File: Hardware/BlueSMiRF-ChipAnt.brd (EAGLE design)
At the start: 41.9 x 16 mm, 27 parts, among them Q1 MOSFET-NCHANNELSMD, Q2 MOSFET-NCHANNELSMD, U1 BLUETOOTH-RN41, U3 3.3V

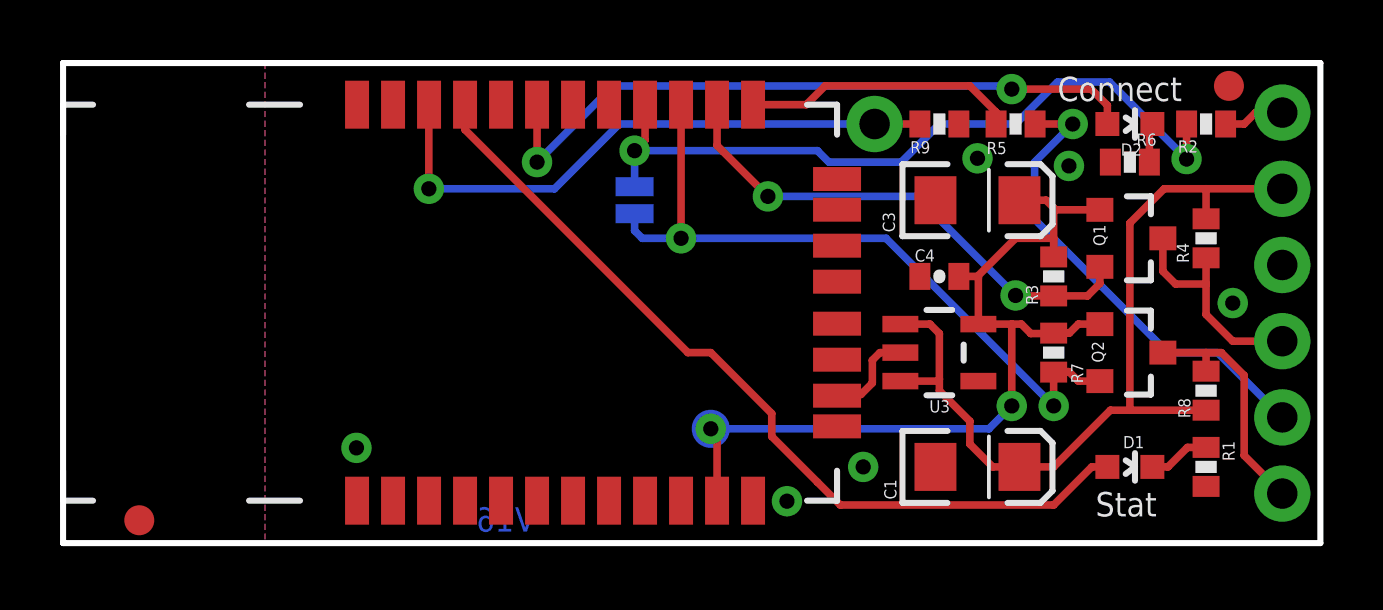
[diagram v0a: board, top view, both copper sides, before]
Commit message: Update RES/CAP packages to 0603
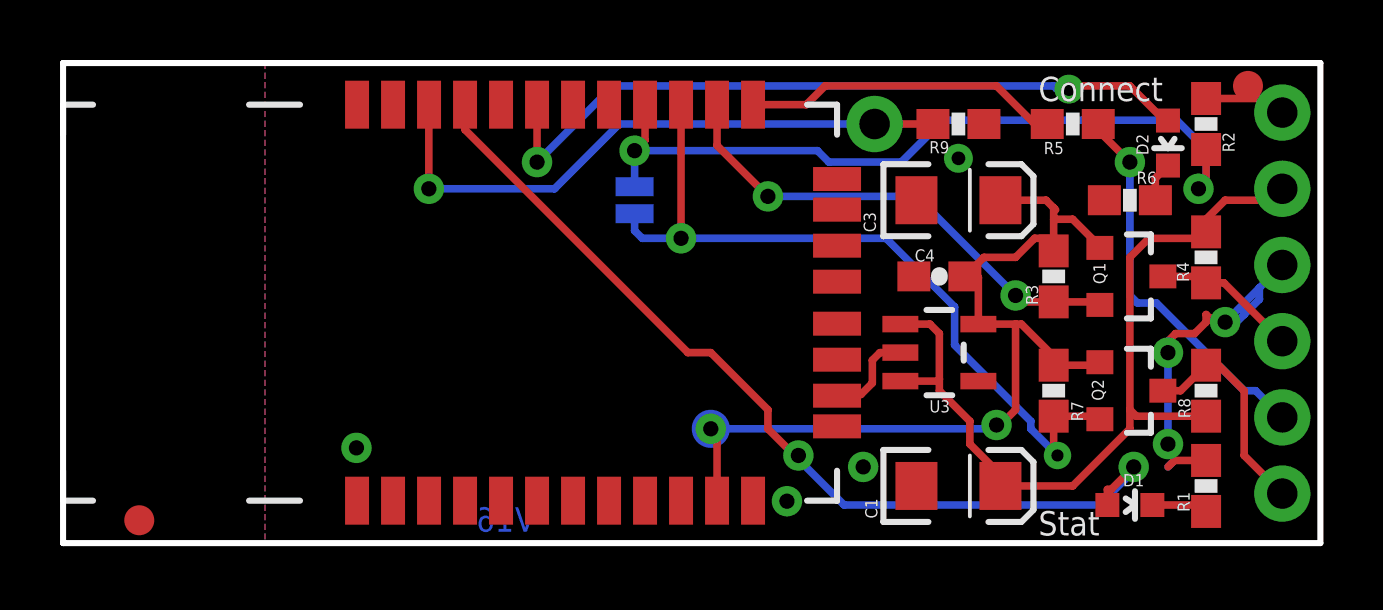
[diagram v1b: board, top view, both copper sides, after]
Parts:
- C4: device SparkFun:0402-CAP -> SparkFun:0603-CAP
- R1, R2, R3, R4, R5, R6, R7, R8, R9: device SparkFun:0402-RES -> SparkFun:0603-RES
- moved R5 1.91 mm to (33.7, 14.0)
- moved D2 1.42 mm to (36.8, 13.3), turned to 180 degrees
- moved D1 1.27 mm to (35.6, 1.27)
- moved Q1 1.27 mm to (35.6, 8.89)
- moved Q2 1.27 mm to (35.6, 5.08)
- moved R6 1.27 mm to (35.6, 11.4)
- moved R7 1.27 mm to (33.0, 5.08)
- moved C1 0.90 mm to (29.8, 1.91)
- moved C3 0.64 mm to (29.8, 11.4)
- moved R1 0.64 mm to (38.1, 1.91), turned to 90 degrees
- moved R4 0.63 mm to (38.1, 9.53)
- moved JP3 0.63 mm to (39.5, 15.2)
- moved R9 0.63 mm to (29.8, 14.0)
- turned R2 to 90 degrees
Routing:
- net GND: track 3.15 -> 14.5 mm, vias 6 -> 7
- net RX_5V: track 15.9 -> 12.9 mm
- net N$1: track 28.4 -> 31.1 mm, vias 0 -> 2
- net TX_5V: track 7.51 -> 4.87 mm
- net 3.3V: track 29.6 -> 31.9 mm
- net RTS: track 24.2 -> 26.1 mm
- net N$2: track 22.9 -> 24.6 mm
- net RX: track 9.12 -> 10.6 mm
- net CTS: track 24.8 -> 25.9 mm
- net CTS_5V: track 2.05 -> 2.73 mm
- net TX: track 16.9 -> 16.3 mm

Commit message: Updated board layout
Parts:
- removed JP3: FIDUCIAL1X2, SparkFun:FIDUCIAL-1X2
- moved D1 2.44 mm to (37.5, 2.79)
- moved R2 1.14 mm to (37.5, 14.9), turned to 0 degrees
- moved R1 0.90 mm to (37.5, 1.27), turned to 180 degrees
- moved D2 0.65 mm to (37.5, 13.5), turned to 90 degrees
- moved R4 0.63 mm to (38.1, 8.89)
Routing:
- net GND: track 14.5 -> 5.69 mm, vias 7 -> 4
- net N$2: track 24.6 -> 28.7 mm
- net 3.3V: track 31.9 -> 28.7 mm
- net CTS: track 25.9 -> 23.5 mm
- net D2: track 1.33 -> 2.57 mm
- net RX_5V: track 12.9 -> 14.0 mm
- net RTS: track 26.1 -> 25.2 mm

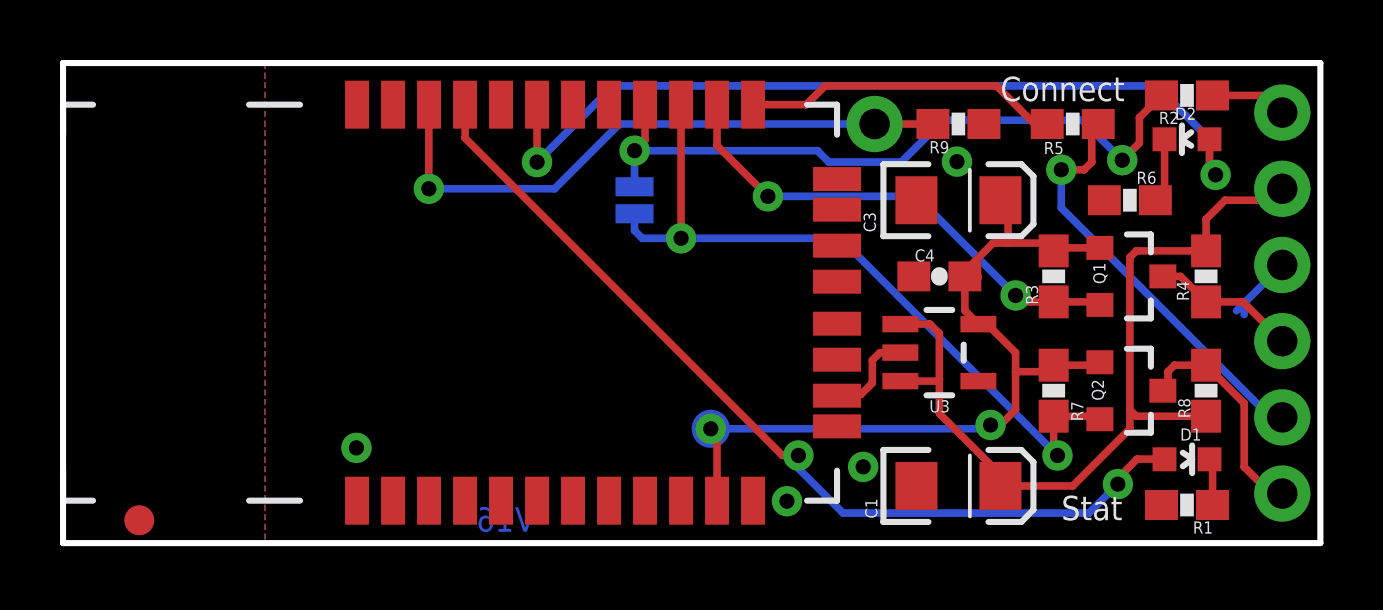
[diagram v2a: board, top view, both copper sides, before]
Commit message: Fixing silk screen positions
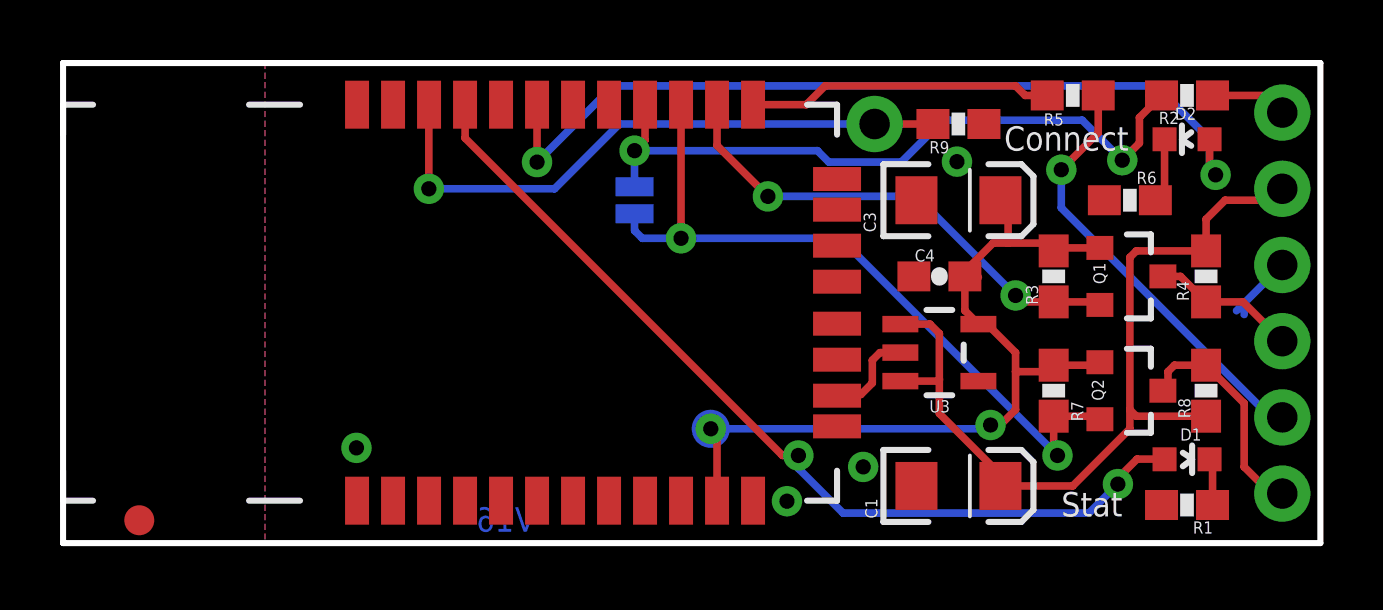
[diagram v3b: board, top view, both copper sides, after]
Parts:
- added U$2: REVISION, SparkFun-Aesthetics:REVISION
- moved R5 0.95 mm to (33.7, 14.9)
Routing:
- net RX_5V: track 14.0 -> 14.5 mm
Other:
- board text added: "J. Lindblom"
- board text added: "T. Klopfenstein"
- board text removed: "J. Lindblom, T. Klopfenstein"
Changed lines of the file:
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@@
 <text x="38.989" y="13.843" size="1.016" layer="22" font="vector" ratio="15" rot="MR0">CTS-I</text>
 <text x="38.989" y="3.683" size="1.016" layer="22" font="vector" ratio="15" rot="MR0">RX-I</text>
-<text x="33.274" y="0.762" size="0.8128" layer="21" font="vector" ratio="15">Stat</text>
-<text x="31.242" y="14.732" size="0.8128" layer="21" font="vector" ratio="15">Connect</text>
+<text x="33.274" y="0.889" size="0.8128" layer="21" font="vector" ratio="15">Stat</text>
+<text x="31.369" y="13.081" size="0.8128" layer="21" font="vector" ratio="15">Connect</text>
 <text x="25.781" y="13.462" size="1.016" layer="22" font="vector" ratio="15" rot="MR0">PIO4</text>
 <text x="15.748" y="0.381" size="0.8128" layer="16" font="vector" ratio="25" rot="MR0">V16</text>
@@
 <text x="17.78" y="11.43" size="0.8128" layer="22" font="vector" ratio="15" rot="MR0">CTS</text>
 <text x="17.78" y="10.16" size="0.8128" layer="22" font="vector" ratio="15" rot="MR0">RTS</text>
-<text x="34.29" y="-8.89" size="1.778" layer="48" font="vector" ratio="15">J. Lindblom, T. Klopfenstein</text>
+<text x="34.29" y="-8.89" size="1.778" layer="48" font="vector" ratio="15">J. Lindblom</text>
+<text x="33.9725" y="-11.43" size="1.778" layer="48" font="vector" ratio="15">T. Klopfenstein</text>
 </plain>
 <attributes>
@@
 <attribute name="VALUE" x="37.1348" y="10.0203" size="0.4064" layer="27" rot="R270"/>
 </element>
-<element name="R5" library="SparkFun" package="0603-RES" value="10K" x="33.655" y="13.97" smashed="yes">
-<attribute name="NAME" x="32.6898" y="12.9667" size="0.4064" layer="25"/>
-<attribute name="VALUE" x="33.6423" y="12.9794" size="0.4064" layer="27"/>
+<element name="R5" library="SparkFun" package="0603-RES" value="10K" x="33.655" y="14.9225" smashed="yes">
+<attribute name="NAME" x="32.6898" y="13.9192" size="0.4064" layer="25"/>
+<attribute name="VALUE" x="33.6423" y="13.9319" size="0.4064" layer="27"/>
 </element>
 <element name="D2" library="SparkFun" package="LED-0603" value="Green" x="37.465" y="13.462" smashed="yes" rot="R90">
@@
 <element name="FRAME1" library="SparkFun-Aesthetics" package="CREATIVE_COMMONS" value="FRAME-LETTER" x="3.067878125" y="-8.89"/>
 <element name="LOGO1" library="SparkFun-Aesthetics" package="OSHW-LOGO-S" value="OSHW-LOGOS" x="17.78" y="3.81" rot="MR0"/>
+<element name="U$2" library="SparkFun-Aesthetics" package="REVISION" value="REVISION" x="14.605" y="-11.43"/>
 </elements>
 <signals>
@@
 <wire x1="22.999" y1="14.614" x2="24.774" y2="14.614" width="0.254" layer="1"/>
 <wire x1="24.774" y1="14.614" x2="25.4" y2="15.24" width="0.254" layer="1"/>
-<wire x1="32.385" y1="13.97" x2="31.115" y2="15.24" width="0.254" layer="1"/>
-<wire x1="31.115" y1="15.24" x2="25.4" y2="15.24" width="0.254" layer="1"/>
-<wire x1="32.805" y1="13.97" x2="32.385" y2="13.97" width="0.254" layer="1"/>
+<wire x1="32.805" y1="14.9225" x2="32.0675" y2="14.9225" width="0.254" layer="1"/>
+<wire x1="32.0675" y1="14.9225" x2="31.75" y2="15.24" width="0.254" layer="1"/>
+<wire x1="31.75" y1="15.24" x2="25.4" y2="15.24" width="0.254" layer="1"/>
 </signal>
 <signal name="RX_5V">
@@
 <contactref element="JP1" pad="5"/>
 <via x="33.274" y="12.446" extent="1-16" drill="0.508"/>
-<wire x1="34.505" y1="13.97" x2="34.505" y2="13.755" width="0.254" layer="1"/>
-<wire x1="34.505" y1="13.755" x2="34.29" y2="13.54" width="0.254" layer="1"/>
-<wire x1="34.29" y1="13.54" x2="34.29" y2="12.7" width="0.254" layer="1"/>
-<wire x1="34.29" y1="12.7" x2="34.036" y2="12.446" width="0.254" layer="1"/>
-<wire x1="34.036" y1="12.446" x2="33.274" y2="12.446" width="0.254" layer="1"/>
 <wire x1="33.274" y1="12.446" x2="33.274" y2="11.176" width="0.254" layer="16"/>
 <wire x1="33.274" y1="11.176" x2="40.259" y2="4.191" width="0.254" layer="16"/>
 <wire x1="40.259" y1="4.191" x2="40.64" y2="4.191" width="0.254" layer="16"/>
+<wire x1="34.505" y1="14.9225" x2="34.505" y2="13.677" width="0.254" layer="1"/>
+<wire x1="34.505" y1="13.677" x2="33.274" y2="12.446" width="0.254" layer="1"/>
 </signal>
 <signal name="VCC">
